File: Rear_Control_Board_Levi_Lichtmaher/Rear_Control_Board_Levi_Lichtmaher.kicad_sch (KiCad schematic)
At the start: 0 parts

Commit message: <Schematic 1st Draft>
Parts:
- added C1, C12, C2, C22, C23, C25, C26, C4, C5, C6, C8, C9: 0.1uF, symbol Device:C_Small
- added C10, C11, C19, C24, C27, C7: 0.1 uF, symbol Device:C_Small
- added C13: 10uF, symbol Device:C_Small
- added C3: 0.1uF, symbol Device:C
- added H1, H2, H3, H4: MountingHole, symbol Mechanical:MountingHole
- added J1, J2, J3, J4, J5, J6, J7, J8: 430450200, SMV_Connectors:CONN_SD-43045-001_02_MOL, symbol SMV_Custom:430450200
- added J10: Molex Micro-Fit 4 Pin, SMV_Connectors:4_pin0430450401, symbol SMV_Custom:Molex Micro-Fit 4 Pin
- added J11, J12, J9: 22035035, SMV_Connectors:3pin_CON_22035035_MOL, symbol SMV_Custom:3-pin Mini Molex Spox
- added Q1, Q2, Q3, Q4: PSMN1R8-40YLC_115, LFPAK56_SOT669_NEX, symbol SMV_Custom:PSMN1R8-40YLC_115
- added R1, R12, R13, R15, R16, R29, R3, R32, R5, R7: 10k, symbol Device:R
- added R10, R30, R9: 100, symbol Device:R
- added R11: 120, symbol Device:R
- added R2, R4, R6, R8: 1K, symbol Device:R
- added R28, R31: 40k, symbol Device:R
- added TP1, TP10, TP11, TP12, TP13, TP14, TP15, TP16, TP17, TP18, TP19, TP2, TP20, TP21, TP22, TP23, TP24, TP25, TP26, TP27, TP28, TP29, TP3, TP30, TP31, TP32, TP33, TP34, TP35, TP36, TP37, TP38, TP39, TP40, TP41, TP6, TP7, TP8, TP9: TestPoint, symbol Connector:TestPoint
- added TP4: CS1, symbol Connector:TestPoint
- added TP5: CS2, symbol Connector:TestPoint
- added U1: ~, symbol SMV_Custom:STM32_Nucleo_F446RE
- added U11, U12, U6: MCP6286T-E/OT, SMV_ICs:SOT-23-5_MC_MCH, symbol SMV_Custom:MCP6286T-E_OT
- added U2: ADS1118QDGSRQ1, DGS0010A_N, symbol SMV_Custom:ADS1118QDGSRQ1
- added U3: MCP2562-E/P, PDIP8_300MC_MCH, symbol SMV_Custom:MCP2562-E_P
- added U4: UA78M05QDCYRG4Q1, SMV_ICs:DCY4_TEX, symbol SMV_Custom:UA78M05QDCYRG4Q1
- added U5: ASM330LHHTR, LGA-14L_2P5X3X0P83_STM, symbol SMV_Custom:ASM330LHHTR
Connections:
- new net: R15.2, R16.1, TP14.1, U6.3 (VIN+)
- new net: R30.2, U12.1 (VOUT), U12.4 (VIN-)
- new net: R31.2, R32.1, TP21.1, U12.3 (VIN+)
- new net: Q3.4 (Gate), R5.1, R6.1
- new net: J7.2, Q3.5 (Drain)
- new net: J4.2, J6.2, Q2.5 (Drain)
- new net: Q1.4 (Gate), R1.1, R2.1
- new net: J3.2, J5.2, Q1.5 (Drain)
- new net: R28.2, R29.1, TP18.1, U11.3 (VIN+)
- new net: R10.2, U11.1 (VOUT), U11.4 (VIN-)
- new net: Q2.4 (Gate), R3.1, R4.1
- new net: Q4.4 (Gate), R7.1, R8.1
- new net: J9.3, R15.1, TP15.1
- new net: R9.2, U6.1 (VOUT), U6.4 (VIN-)
- new net: J8.2, Q4.5 (Drain)
- new net +12V: C1.1, C8.1, J1.1, J10.1, J2.1, J3.1, J4.1, J5.1, J6.1, J7.1, J8.1, TP29.1, TP3.1, TP30.1, TP31.1, TP32.1, TP33.1, TP34.1, TP36.1, TP37.1, U4.3 (INPUT)
- new net +3.3V: C10.1, C11.1, C12.1, C13.1, C19.1, C2.1, C24.1, C27.1, C4.1, C5.1, R12.1, R13.1, TP1.1, TP10.1, TP11.1, TP13.1, TP16.1, TP17.1, TP20.1, TP22.1, TP6.1, U1.16 (+3V3), U1.45 (AVDD), U11.5 (VDD), U12.5 (VDD), U2.8 (VDD), U3.5 (VIO), U5.2 (RES), U5.3 (RES), U5.5 (VDD_IO), U5.8 (VDD), U6.5 (VDD)
- new net +5V: C25.1, C3.1, C6.1, C7.1, C9.1, J9.1, TP12.1, TP2.1, TP28.1, TP7.1, TP9.1, U1.18 (+5V), U1.5 (VDD), U3.3 (VDD), U4.1 (OUTPUT)
- new net 1: J11.1, J12.1, R11.2, U3.6 (CANL)
- new net AIN0: U2.4 (AIN0)
- new net CS1: R13.2, TP4.1, U1.54 (PB12), U2.2 (CS_N)
- new net CS2: R12.2, TP5.1, U1.65 (PB4), U5.12 (CS)
- new net GND: C1.2, C10.2, C11.2, C12.2, C13.2, C19.2, C2.2, C22.2, C23.2, C24.2, C25.2, C26.2, C27.2, C3.2, C4.2, C5.2, C6.2, C7.2, C8.2, C9.2, J1.2, J10.3, J11.2, J12.2, J2.2, J9.2, Q1.1 (Source_1), Q1.2 (Source_2), Q1.3 (Source_3), Q2.1 (Source_1), Q2.2 (Source_2), Q2.3 (Source_3), Q3.1 (Source_1), Q3.2 (Source_2), Q3.3 (Source_3), Q4.1 (Source_1), Q4.2 (Source_2), Q4.3 (Source_3), R1.2, R16.2, R29.2, R3.2, R32.2, R5.2, R7.2, TP19.1, TP35.1, TP38.1, TP39.1, TP40.1, TP41.1, TP8.1, U1.19 (GND), U1.20 (GND), U1.22 (GND), U1.47 (GND), U1.58 (GND), U1.70 (AGND), U1.8 (GND), U11.2 (VSS), U12.2 (VSS), U2.3 (GND), U2.7 (AIN3), U3.2 (VSS), U3.8 (STBY), U4.2 (GND), U4.4 (GND), U5.6 (GND), U5.7 (GND), U6.2 (VSS)
- new net H: J11.3, J12.3, R11.1, U3.7 (CANH)
- new net MISO: U1.66 (PB14), U2.9 (DOUT_DRDY_N), U5.1 (SDO/SA0)
- new net MOSI: U1.64 (PB15), U2.10 (DIN), U5.14 (SDA)
- new net PA8: R4.2, U1.61 (PA8)
- new net PB10: R8.2, U1.63 (PB10)
- new net PB3: R6.2, U1.69 (PB3)
- new net PB5: R2.2, U1.67 (PB5)
- new net Pressure: C22.1, R9.1, TP23.1
- new net RD: U1.41 (PB8), U3.4 (RXD)
- new net SCK: U1.68 (PB13), U2.1 (SCLK), U5.13 (SCL)
- new net TD: U1.43 (PB9), U3.1 (TXD)
- new net Torque_N: J10.4, R28.1, TP27.1
- new net Torque_N_ADC: C23.1, R10.1, TP24.1, U2.5 (AIN1)
- new net Torque_P: J10.2, R31.1, TP26.1
- new net Torque_P_ADC: C26.1, R30.1, TP25.1, U2.6 (AIN2)
- no-connect marks 0 -> 48
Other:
- note added: "12V-2.4V"
- note added: "5V-2.5V"
- note added: "ADC"
- note added: "Accelerometer"
- note added: "Brake Light Connector #1"
- note added: "Brake Light Connector #2"
- note added: "CAN Connector"
- note added: "CAN Tranciever"
- note added: "LDO"
- note added: "Left Side Power Connector"
- note added: "Mosfet"
- note added: "N"
- note added: "Op-Amp"
- note added: "P"
- note added: "Pressure Sensor Buffer"
- note added: "Pressure Sensor Connector"
- note added: "Right Side Power Connector"
- note added: "STM32"
- note added: "Tail Light Connector #1"
- note added: "Tail Light Connector #2"
- note added: "Torque Sensor Connector"
- note added: "Torque Sensor N Buffer"
- note added: "Torque Sensor P Buffer"
- note added: "Turn Signal Light Connector #1"
- note added: "Turn Signal Light Connector #2"

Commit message: please push
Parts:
- removed C25: 0.1uF, symbol Device:C_Small
- removed TP28, TP3, TP38, TP39, TP41, TP8: TestPoint, symbol Connector:TestPoint
- added R14, R17, R18: 50, symbol Device:R
- added TP42, TP43, TP44: TestPoint, symbol Connector:TestPoint
- R11: value 120 -> 0
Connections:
- net AIN0 is gone; now on net Pressure: U2.4 (AIN0)
- net +3.3V: now also C6.1, R11.1, TP12.1, U1.5 (VDD), TP42.1
- net +5V: no longer C6.1, TP12.1, U1.18 (+5V), U1.5 (VDD)
- net GND: now also TP43.1, TP44.1; no longer TP35.1, U2.7 (AIN3)
- net MISO: now also R17.2; no longer U1.66 (PB14)
- net MOSI: now also R14.2; no longer U1.64 (PB15)
- net SCK: now also R18.2; no longer U1.68 (PB13)
- net at U1.33 (VBAT): now also R11.2
- net 1 renamed CAN_N
- net CAN_N: no longer R11.2
- net H renamed CAN_P
- net CAN_P: no longer R11.1
- new net: R14.1, U1.64 (PB15)
- new net: R17.1, U1.66 (PB14)
- new net: R18.1, U1.68 (PB13)
- new net +2V5: TP35.1, U2.7 (AIN3)
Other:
- moved on the sheet: C23, C24, C8, J10, R10, R28, R29, TP17, TP18, TP19, TP24, TP27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

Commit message: implemented feedback #2 - need to look into differential op-amps
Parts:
- removed TP1, TP10, TP11, TP13, TP16, TP17, TP19, TP20, TP22, TP23, TP24, TP25, TP29, TP30, TP31, TP32, TP33, TP34, TP42, TP6, TP9: TestPoint, symbol Connector:TestPoint
- removed TP4: CS1, symbol Connector:TestPoint
- removed TP5: CS2, symbol Connector:TestPoint
- added C14: 0.1uF, symbol Device:C_Small
- added R19, R20: 50, symbol Device:R
- TP12: value TestPoint -> 3V3
- TP14, TP35: value TestPoint -> 2V5
- TP15: value TestPoint -> 5V Pressure Sensor
- TP18, TP21: value TestPoint -> 2.4V
- TP2, TP7: value TestPoint -> 5V
- TP26: value TestPoint -> 12V Torque_P
- TP27: value TestPoint -> 12V Torque_N
- TP36, TP37: value TestPoint -> 12V
- TP40, TP43, TP44: value TestPoint -> GND
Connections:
- net CS1: now also R20.2; no longer U1.54 (PB12)
- net CS2: now also R19.2; no longer U1.65 (PB4)
- net GND: now also C14.2
- net +3.3V renamed +3V3
- net +3V3: now also C14.1
- net PA8 renamed Brake Lights
- net PB10 renamed Turn Signal Light 2
- net PB3 renamed Turn Signal Light 1
- net PB5 renamed Tail Lights
- net RD renamed RX
- net TD renamed TX
- new net: R20.1, U1.54 (PB12)
- new net: R19.1, U1.65 (PB4)
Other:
- moved on the sheet: C1, C19, C22, C23, C24, C26, C27, C3, C7, C8, J10, J9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

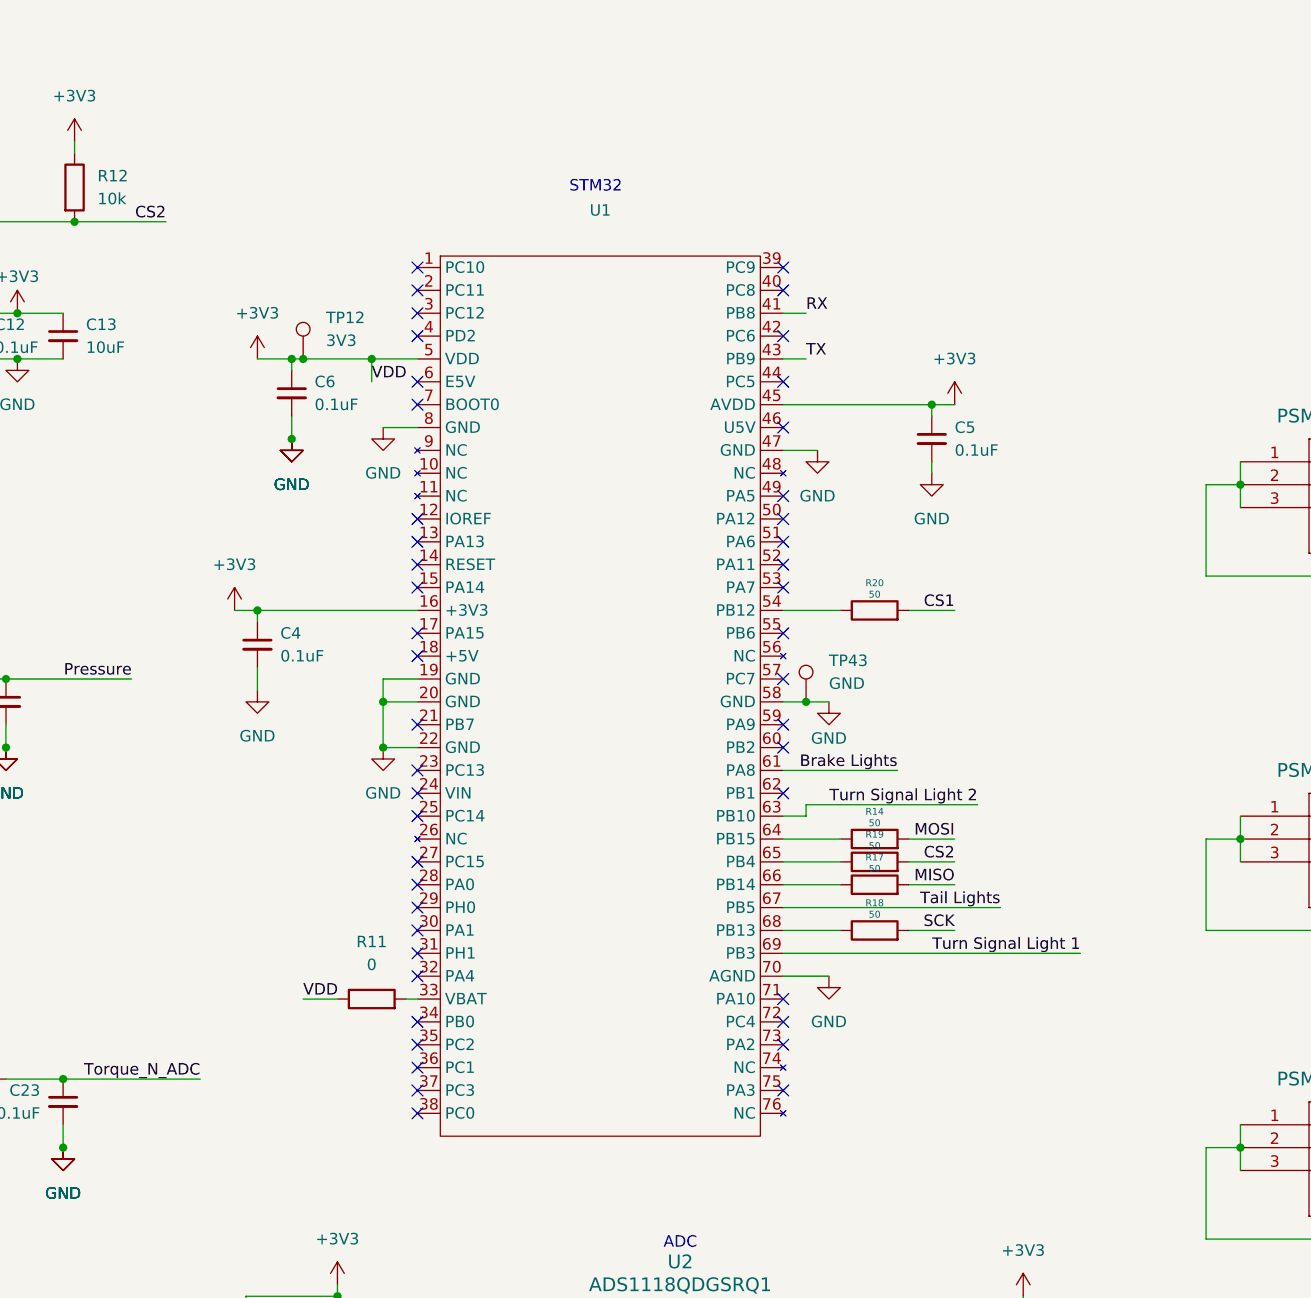
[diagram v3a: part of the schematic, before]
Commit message: Updated STM32 symbol to align with footprint
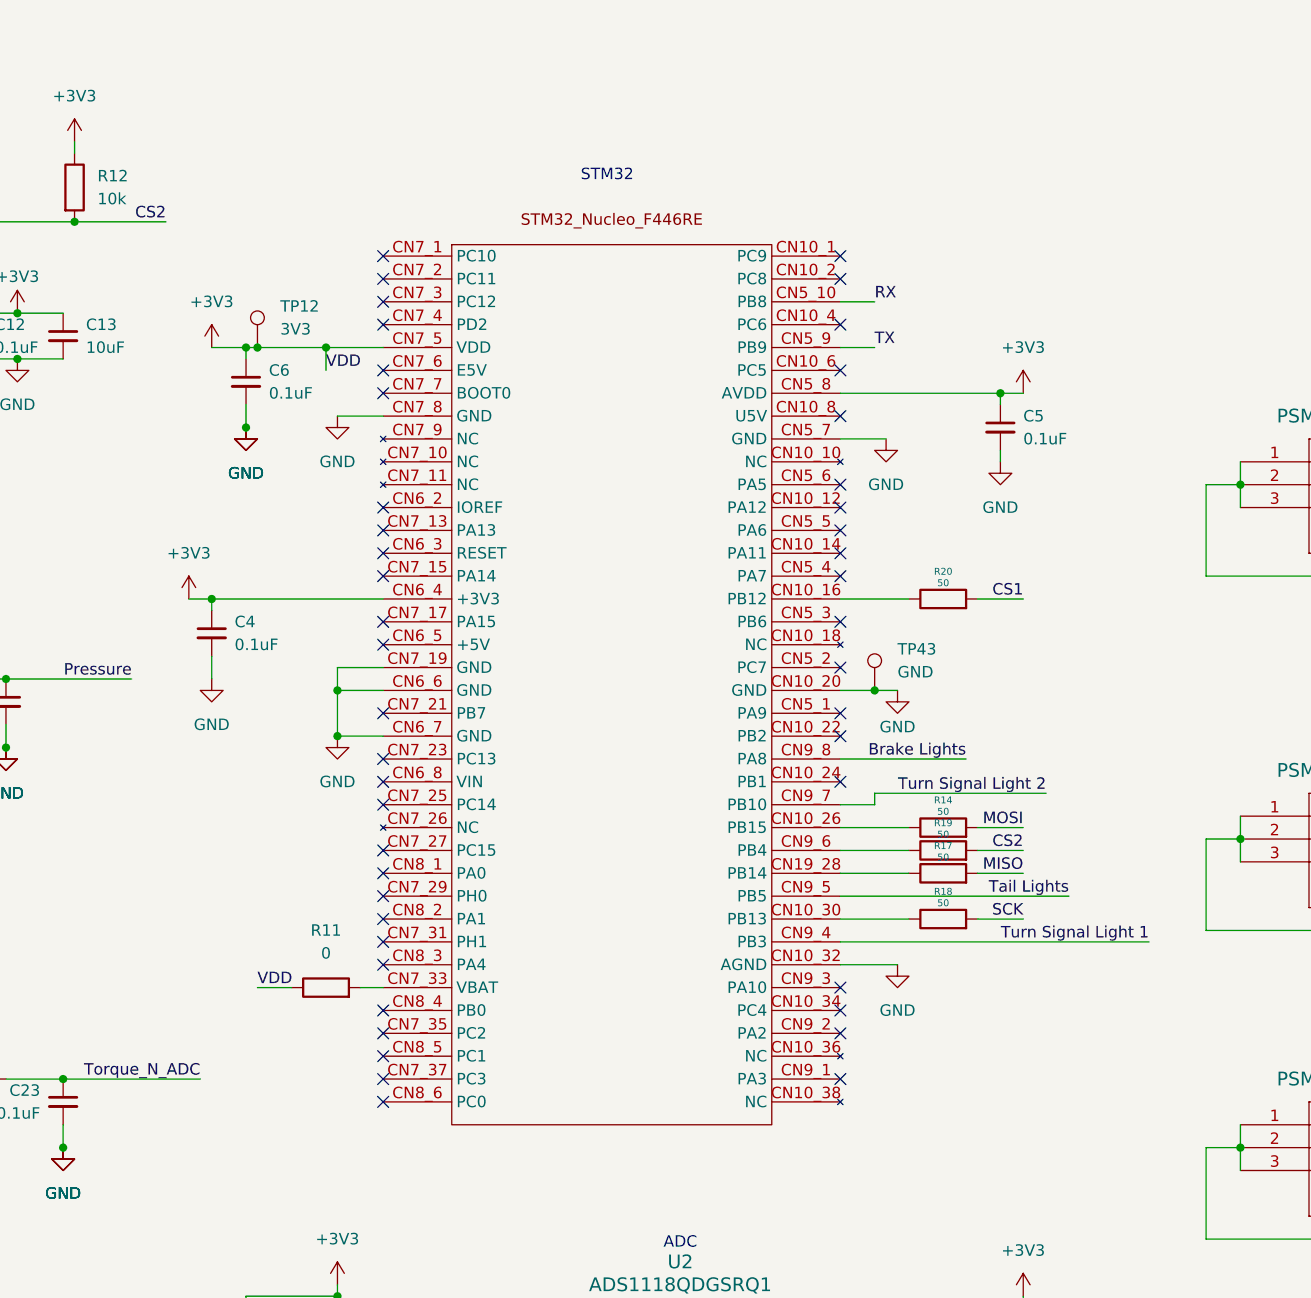
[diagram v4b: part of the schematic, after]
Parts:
- removed U1: ~, symbol SMV_Custom:STM32_Nucleo_F446RE
- added U7: ~, SMV_ICs:MODULE_NUCLEO-F446RE, symbol SMV_Custom:STM32_Nucleo_F446RE
- C1, C10, C11, C12, C13, C14, C19, C2, C22, C23, C24, C26, C27, C3, C4, C5, C6, C7, C8, C9: footprint (none) -> Capacitor_SMD:C_0805_2012Metric
- H1, H2, H3, H4: footprint (none) -> MountingHole:MountingHole_3.2mm_M3
- Q2: footprint LFPAK56_SOT669_NEX -> SMV_ICs:LFPAK56_SOT669_NEX-mosfet
- R1, R10, R11, R12, R13, R14, R15, R16, R17, R18, R19, R2, R20, R28, R29, R3, R30, R31, R32, R4, R5, R6, R7, R8, R9: footprint (none) -> Resistor_SMD:R_0805_2012Metric
- TP12, TP14, TP15, TP18, TP2, TP21, TP26, TP27, TP35, TP36, TP37, TP40, TP43, TP44, TP7: footprint (none) -> TestPoint:TestPoint_Pad_D1.0mm
- U5: footprint LGA-14L_2P5X3X0P83_STM -> SMV_ICs:QFN_LHHXTR_STM
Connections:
- net +3V3: now also U7.CN5_8 (AVDD), U7.CN6_4 (+3V3), U7.CN7_5 (VDD)
- net Brake Lights: now also U7.CN9_8 (PA8)
- net GND: now also U7.CN10_20 (GND), U7.CN10_32 (AGND), U7.CN5_7 (GND), U7.CN6_6 (GND), U7.CN6_7 (GND), U7.CN7_19 (GND), U7.CN7_8 (GND)
- net RX: now also U7.CN5_10 (PB8)
- net TX: now also U7.CN5_9 (PB9)
- net Tail Lights: now also U7.CN9_5 (PB5)
- net Turn Signal Light 1: now also U7.CN9_4 (PB3)
- net Turn Signal Light 2: now also U7.CN9_7 (PB10)
- net at R20.1: now also U7.CN10_16 (PB12)
- net at R11.2: now also U7.CN7_33 (VBAT)
- net at R14.1: now also U7.CN10_26 (PB15)
- net at R19.1: now also U7.CN9_6 (PB4)
- net at R17.1: now also U7.CN19_28 (PB14)
- net at R18.1: now also U7.CN10_30 (PB13)
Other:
- moved on the sheet: C4, C5, C6, R11, R14, R17, R18, R19, R20, TP12, TP43

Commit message: first draft PCB
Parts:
- Q1, Q3, Q4: footprint LFPAK56_SOT669_NEX -> SMV_ICs:LFPAK56_SOT669_NEX-mosfet
- U3: footprint PDIP8_300MC_MCH -> SMV_ICs:SOIC127P600X175-8N
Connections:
- net +3V3: now also U7.CN10_7 (AVDD), U7.CN7_16 (+3V3); no longer U7.CN5_8 (AVDD), U7.CN6_4 (+3V3)
- net Brake Lights: now also U7.CN7_31 (PH1); no longer U7.CN9_8 (PA8)
- net GND: now also U7.CN10_9 (GND), U7.CN7_20 (GND), U7.CN7_22 (GND); no longer U7.CN5_7 (GND), U7.CN6_6 (GND), U7.CN6_7 (GND)
- net Pressure: now also U2.6 (AIN2); no longer U2.4 (AIN0)
- net RX: now also U7.CN10_3 (PB8); no longer U7.CN5_10 (PB8)
- net TX: now also U7.CN10_5 (PB9); no longer U7.CN5_9 (PB9)
- net Tail Lights: now also U7.CN7_13 (PA13); no longer U7.CN9_5 (PB5)
- net Torque_P_ADC: now also U2.4 (AIN0); no longer U2.6 (AIN2)
- net Turn Signal Light 1: now also U7.CN7_15 (PA14); no longer U7.CN9_4 (PB3)
- net Turn Signal Light 2: now also U7.CN7_21 (PB7); no longer U7.CN9_7 (PB10)
- net at R17.1: now also U7.CN10_28 (PB14); no longer U7.CN19_28 (PB14)
- net at R19.1: now also U7.CN10_27 (PB4); no longer U7.CN9_6 (PB4)
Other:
- moved on the sheet: C4, C5, C6, R11, R14, R17, R18, R19, R20, TP12, TP43

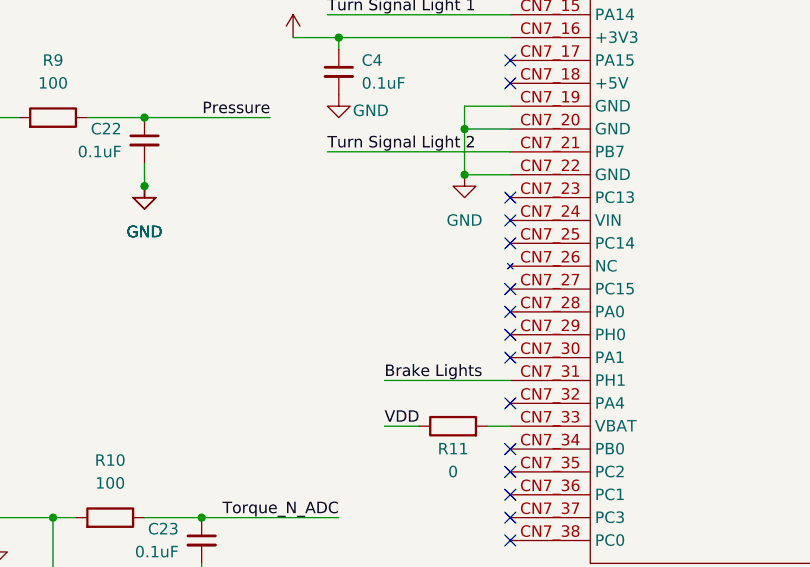
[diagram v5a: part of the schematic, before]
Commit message: added LED for testing
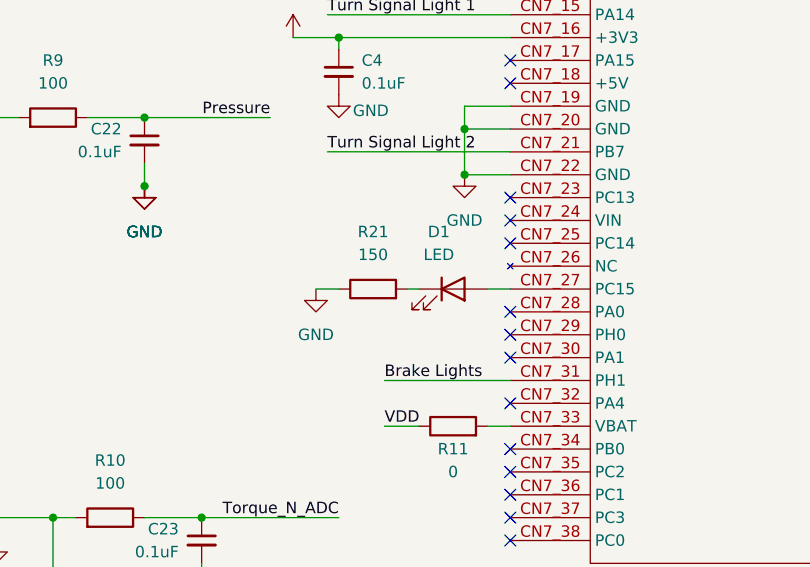
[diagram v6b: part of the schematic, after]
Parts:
- added D1: LED, SMV_Passives:WL-SMCW_0603(diode), symbol Device:LED
- added R21: 150, Resistor_SMD:R_0805_2012Metric, symbol Device:R
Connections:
- net GND: now also R21.1
- net at U7.CN7_27 (PC15): now also D1.2 (A)
- new net: D1.1 (K), R21.2
- no-connect marks 48 -> 47
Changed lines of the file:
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@@
 	)
 	(no_connect
-		(at 232.41 149.86)
-	)
-	(no_connect
 		(at 232.41 111.76)
 	)
@@
 	(wire
 		(pts
+			(xy 210.82 149.86) (xy 213.36 149.86)
+		)
+		(stroke
+			(width 0)
+			(type default)
+		)
+	)
+	(wire
+		(pts
 			(xy 81.28 167.64) (xy 81.28 170.18)
 		)
@@
 	(wire
 		(pts
+			(xy 229.87 149.86) (xy 232.41 149.86)
+		)
+		(stroke
+			(width 0)
+			(type default)
+		)
+	)
+	(wire
+		(pts
 			(xy 81.28 179.07) (xy 81.28 180.34)
 		)
@@
 	(wire
 		(pts
+			(xy 220.98 149.86) (xy 222.25 149.86)
+		)
+		(stroke
+			(width 0)
+			(type default)
+		)
+	)
+	(wire
+		(pts
 			(xy 328.93 146.05) (xy 328.93 148.59)
 		)
@@
 	)
 	(symbol
+		(lib_id "Device:R")
+		(at 217.17 149.86 90)
+		(unit 1)
+		(exclude_from_sim no)
+		(in_bom yes)
+		(on_board yes)
+		(dnp no)
+		(fields_autoplaced yes)
+		(property "Reference" "R21"
+			(at 217.17 143.51 90)
+			(effects
+				(font
+					(size 1.27 1.27)
+				)
+			)
+		)
+		(property "Value" "150"
+			(at 217.17 146.05 90)
+			(effects
+				(font
+					(size 1.27 1.27)
+				)
+			)
+		)
+		(property "Footprint" "Resistor_SMD:R_0805_2012Metric"
+			(at 217.17 151.638 90)
+			(effects
+				(font
+					(size 1.27 1.27)
+				)
+				(hide yes)
+			)
+		)
+		(property "Datasheet" "~"
+			(at 217.17 149.86 0)
+			(effects
+				(font
+					(size 1.27 1.27)
+				)
+				(hide yes)
+			)
+		)
+		(property "Description" "Resistor"
+			(at 217.17 149.86 0)
+			(effects
+				(font
+					(size 1.27 1.27)
+				)
+				(hide yes)
+			)
+		)
+		(pin "1"
+		)
+		(pin "2"
+		)
+		(instances
+			(project ""
+				(path "/04c1ffb8-0232-4390-a852-cf9026a840a3"
+					(reference "R21")
+					(unit 1)
+				)
+			)
+		)
+	)
+	(symbol
 		(lib_id "power:GND")
 		(at 25.4 73.66 0)
@@
 	)
 	(symbol
+		(lib_id "Device:LED")
+		(at 226.06 149.86 0)
+		(unit 1)
+		(exclude_from_sim no)
+		(in_bom yes)
+		(on_board yes)
+		(dnp no)
+		(fields_autoplaced yes)
+		(property "Reference" "D1"
+			(at 224.4725 143.51 0)
+			(effects
+				(font
+					(size 1.27 1.27)
+				)
+			)
+		)
+		(property "Value" "LED"
+			(at 224.4725 146.05 0)
+			(effects
+				(font
+					(size 1.27 1.27)
+				)
+			)
+		)
+		(property "Footprint" "SMV_Passives:WL-SMCW_0603(diode)"
+			(at 226.06 149.86 0)
+			(effects
+				(font
+					(size 1.27 1.27)
+				)
+				(hide yes)
+			)
+		)
+		(property "Datasheet" "~"
+			(at 226.06 149.86 0)
+			(effects
+				(font
+					(size 1.27 1.27)
+				)
+				(hide yes)
+			)
+		)
+		(property "Description" "Light emitting diode"
+			(at 226.06 149.86 0)
+			(effects
+				(font
+					(size 1.27 1.27)
+				)
+				(hide yes)
+			)
+		)
+		(property "Sim.Pins" "1=K 2=A"
+			(at 226.06 149.86 0)
+			(effects
+				(font
+					(size 1.27 1.27)
+				)
+				(hide yes)
+			)
+		)
+		(pin "2"
+		)
+		(pin "1"
+		)
+		(instances
+			(project ""
+				(path "/04c1ffb8-0232-4390-a852-cf9026a840a3"
+					(reference "D1")
+					(unit 1)
+				)
+			)
+		)
+	)
+	(symbol
 		(lib_id "Device:R")
 		(at 297.18 147.32 90)
@@
 					(unit 1)
 				)
+			)
+		)
+	)
+	(symbol
+		(lib_id "power:GND")
+		(at 210.82 149.86 0)
+		(unit 1)
+		(exclude_from_sim no)
+		(in_bom yes)
+		(on_board yes)
+		(dnp no)
+		(fields_autoplaced yes)
+		(property "Reference" "#PWR013"
+			(at 210.82 156.21 0)
+			(effects
+				(font
+					(size 1.27 1.27)
+				)
+				(hide yes)
+			)
+		)
+		(property "Value" "GND"
+			(at 210.82 154.94 0)
+			(effects
+				(font
+					(size 1.27 1.27)
+				)
+			)
+		)
+		(property "Footprint" ""
+			(at 210.82 149.86 0)
+			(effects
+				(font
+					(size 1.27 1.27)
+				)
+				(hide yes)
+			)
+		)
+		(property "Datasheet" ""
+			(at 210.82 149.86 0)
+			(effects
+				(font
+					(size 1.27 1.27)
+				)
+				(hide yes)
+			)
+		)
+		(property "Description" "Power symbol creates a global label with name \"GND\" , ground"
+			(at 210.82 149.86 0)
+			(effects
+				(font
+					(size 1.27 1.27)
+				)
+				(hide yes)
+			)
+		)
+		(pin "1"
+		)
+		(instances
+			(project ""
+				(path "/04c1ffb8-0232-4390-a852-cf9026a840a3"
+					(reference "#PWR013")
+					(unit 1)
+				)
